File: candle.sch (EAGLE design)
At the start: 337 parts, among them U1 ATXMEGA_E5_TQFP, U3 S25FL, U4 STP16CPC26TSSOP24

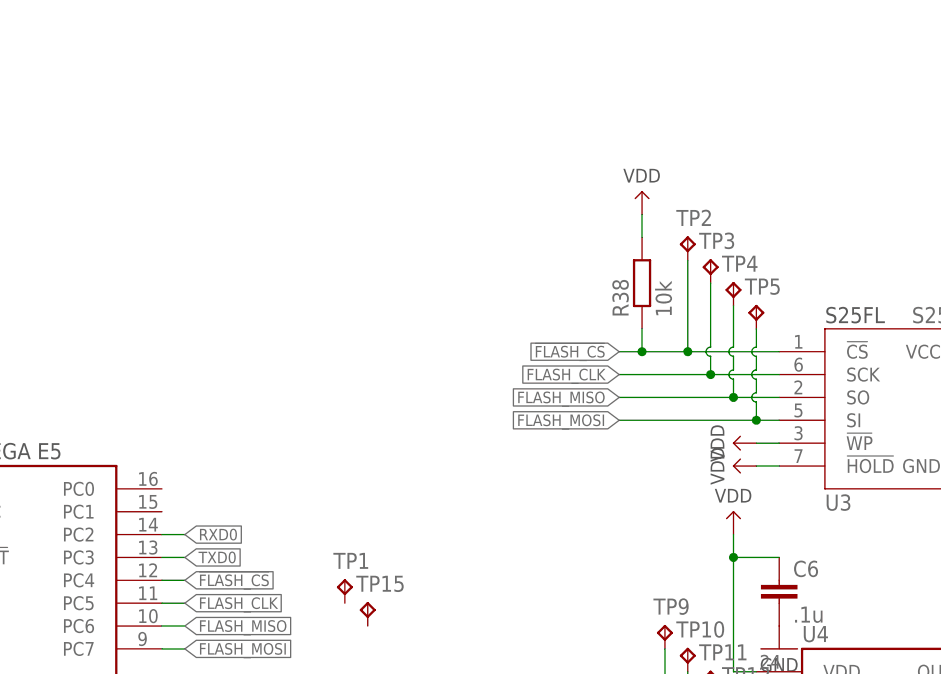
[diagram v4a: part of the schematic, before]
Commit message: Added some todos and verified the flash foodprint
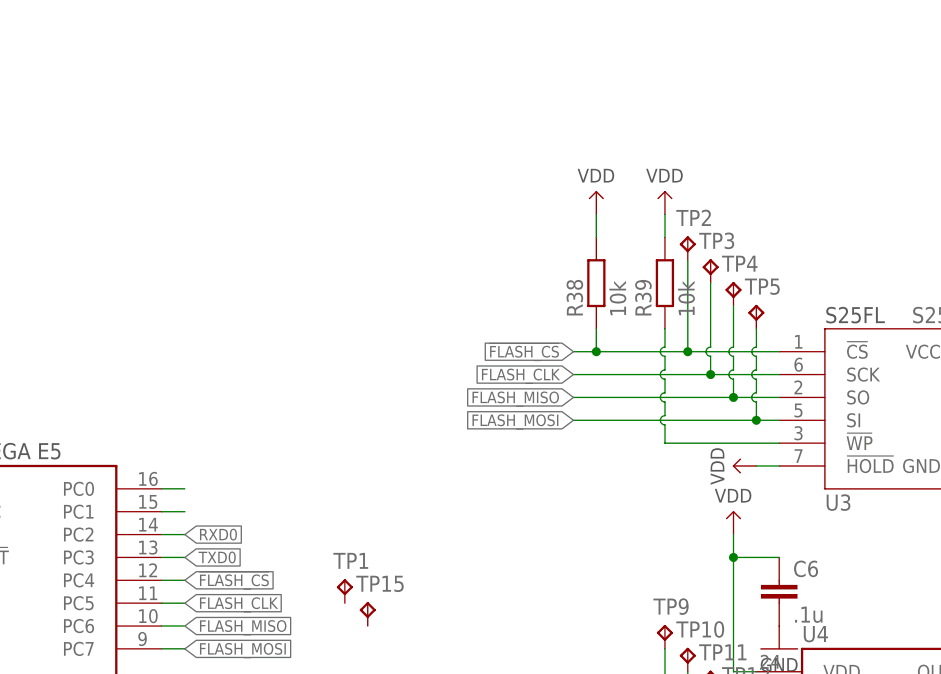
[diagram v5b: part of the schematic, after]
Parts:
- added R39: 10k, Sebastian 2:R_0603
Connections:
- new net N$15: U1.PC1
- new net N$16: U1.PC0
- new net N$6: R39.1, U3.!WP
- net VDD: now also R39.2; no longer U3.!WP
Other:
- moved on the sheet: R38
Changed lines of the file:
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@@
 <part name="P40" library="aesthetics" deviceset="VDD" device=""/>
 <part name="TP16" library="testpad" deviceset="TP" device="B1,27"/>
-<part name="P4" library="aesthetics" deviceset="VDD" device=""/>
 <part name="P5" library="aesthetics" deviceset="VDD" device=""/>
+<part name="R39" library="Sebastian 2" deviceset="R" device="_0603" value="10k"/>
+<part name="P4" library="aesthetics" deviceset="VDD" device=""/>
 </parts>
 <sheets>
@@
 <instance part="TP7" gate="G$1" x="-149.86" y="-91.44" rot="R90"/>
 <instance part="TP8" gate="G$1" x="-132.08" y="-91.44" rot="R270"/>
-<instance part="R38" gate="G$1" x="-78.74" y="30.48" rot="R90"/>
-<instance part="P40" gate="G$1" x="-78.74" y="38.1"/>
+<instance part="R38" gate="G$1" x="-83.82" y="30.48" rot="R90"/>
+<instance part="P40" gate="G$1" x="-83.82" y="38.1"/>
 <instance part="TP16" gate="G$1" x="-68.58" y="-33.02"/>
-<instance part="P4" gate="G$1" x="-66.04" y="12.7" rot="R90"/>
 <instance part="P5" gate="G$1" x="-66.04" y="10.16" rot="R90"/>
+<instance part="R39" gate="G$1" x="-76.2" y="30.48" rot="R90"/>
+<instance part="P4" gate="G$1" x="-76.2" y="38.1"/>
 </instances>
 <busses>
@@
 <segment>
 <pinref part="R38" gate="G$1" pin="2"/>
-<wire x1="-78.74" y1="38.1" x2="-78.74" y2="35.56" width="0.1524" layer="91"/>
+<wire x1="-83.82" y1="38.1" x2="-83.82" y2="35.56" width="0.1524" layer="91"/>
 <pinref part="P40" gate="G$1" pin="VDD"/>
 </segment>
 <segment>
-<pinref part="U3" gate="G$1" pin="!WP"/>
-<wire x1="-63.5" y1="12.7" x2="-66.04" y2="12.7" width="0.1524" layer="91"/>
-<pinref part="P4" gate="G$1" pin="VDD"/>
-</segment>
-<segment>
 <pinref part="U3" gate="G$1" pin="!HOLD"/>
 <wire x1="-63.5" y1="10.16" x2="-66.04" y2="10.16" width="0.1524" layer="91"/>
 <pinref part="P5" gate="G$1" pin="VDD"/>
 </segment>
+<segment>
+<pinref part="R39" gate="G$1" pin="2"/>
+<wire x1="-76.2" y1="38.1" x2="-76.2" y2="35.56" width="0.1524" layer="91"/>
+<pinref part="P4" gate="G$1" pin="VDD"/>
+</segment>
 </net>
 <net name="DISP_CLK" class="0">
@@
 <pinref part="U3" gate="G$1" pin="SCK"/>
 <wire x1="-63.5" y1="20.32" x2="-71.12" y2="20.32" width="0.1524" layer="91"/>
-<label x="-81.28" y="20.32" size="1.27" layer="95" font="vector" rot="R180" xref="yes"/>
+<label x="-86.36" y="20.32" size="1.27" layer="95" font="vector" rot="R180" xref="yes"/>
 <pinref part="TP3" gate="G$1" pin="TP"/>
-<wire x1="-71.12" y1="20.32" x2="-81.28" y2="20.32" width="0.1524" layer="91"/>
+<wire x1="-71.12" y1="20.32" x2="-86.36" y2="20.32" width="0.1524" layer="91"/>
 <wire x1="-71.12" y1="30.48" x2="-71.12" y2="23.368" width="0.1524" layer="91"/>
 <wire x1="-71.12" y1="23.368" x2="-71.628" y2="22.86" width="0.1524" layer="91" curve="90"/>
@@
 <pinref part="U3" gate="G$1" pin="SI"/>
 <wire x1="-63.5" y1="15.24" x2="-66.04" y2="15.24" width="0.1524" layer="91"/>
-<label x="-81.28" y="15.24" size="1.27" layer="95" font="vector" rot="R180" xref="yes"/>
+<label x="-86.36" y="15.24" size="1.27" layer="95" font="vector" rot="R180" xref="yes"/>
 <pinref part="TP5" gate="G$1" pin="TP"/>
-<wire x1="-66.04" y1="15.24" x2="-81.28" y2="15.24" width="0.1524" layer="91"/>
+<wire x1="-66.04" y1="15.24" x2="-86.36" y2="15.24" width="0.1524" layer="91"/>
 <wire x1="-66.04" y1="25.4" x2="-66.04" y2="23.368" width="0.1524" layer="91"/>
 <wire x1="-66.04" y1="23.368" x2="-66.548" y2="22.86" width="0.1524" layer="91" curve="90"/>
@@
 <pinref part="U3" gate="G$1" pin="!CS"/>
 <wire x1="-63.5" y1="22.86" x2="-73.66" y2="22.86" width="0.1524" layer="91"/>
-<label x="-81.28" y="22.86" size="1.27" layer="95" font="vector" rot="R180" xref="yes"/>
+<label x="-86.36" y="22.86" size="1.27" layer="95" font="vector" rot="R180" xref="yes"/>
 <pinref part="TP2" gate="G$1" pin="TP"/>
-<wire x1="-73.66" y1="22.86" x2="-78.74" y2="22.86" width="0.1524" layer="91"/>
-<wire x1="-78.74" y1="22.86" x2="-81.28" y2="22.86" width="0.1524" layer="91"/>
+<wire x1="-73.66" y1="22.86" x2="-83.82" y2="22.86" width="0.1524" layer="91"/>
+<wire x1="-83.82" y1="22.86" x2="-86.36" y2="22.86" width="0.1524" layer="91"/>
 <wire x1="-73.66" y1="33.02" x2="-73.66" y2="22.86" width="0.1524" layer="91"/>
 <junction x="-73.66" y="22.86"/>
 <pinref part="R38" gate="G$1" pin="1"/>
-<wire x1="-78.74" y1="25.4" x2="-78.74" y2="22.86" width="0.1524" layer="91"/>
-<junction x="-78.74" y="22.86"/>
+<wire x1="-83.82" y1="25.4" x2="-83.82" y2="22.86" width="0.1524" layer="91"/>
+<junction x="-83.82" y="22.86"/>
 </segment>
 <segment>
@@
 <pinref part="U3" gate="G$1" pin="SO"/>
 <wire x1="-63.5" y1="17.78" x2="-68.58" y2="17.78" width="0.1524" layer="91"/>
-<label x="-81.28" y="17.78" size="1.27" layer="95" font="vector" rot="R180" xref="yes"/>
+<label x="-86.36" y="17.78" size="1.27" layer="95" font="vector" rot="R180" xref="yes"/>
 <pinref part="TP4" gate="G$1" pin="TP"/>
-<wire x1="-68.58" y1="17.78" x2="-81.28" y2="17.78" width="0.1524" layer="91"/>
+<wire x1="-68.58" y1="17.78" x2="-86.36" y2="17.78" width="0.1524" layer="91"/>
 <wire x1="-68.58" y1="27.94" x2="-68.58" y2="23.368" width="0.1524" layer="91"/>
 <wire x1="-68.58" y1="23.368" x2="-69.088" y2="22.86" width="0.1524" layer="91" curve="90"/>
@@
 </segment>
 </net>
+<net name="N$6" class="0">
+<segment>
+<pinref part="U3" gate="G$1" pin="!WP"/>
+<pinref part="R39" gate="G$1" pin="1"/>
+<wire x1="-76.2" y1="25.4" x2="-76.2" y2="23.368" width="0.1524" layer="91"/>
+<wire x1="-76.2" y1="23.368" x2="-76.708" y2="22.86" width="0.1524" layer="91" curve="90"/>
+<wire x1="-76.708" y1="22.86" x2="-76.2" y2="22.352" width="0.1524" layer="91" curve="90"/>
+<wire x1="-76.2" y1="22.352" x2="-76.2" y2="20.828" width="0.1524" layer="91"/>
+<wire x1="-76.2" y1="20.828" x2="-76.708" y2="20.32" width="0.1524" layer="91" curve="90"/>
+<wire x1="-76.708" y1="20.32" x2="-76.2" y2="19.812" width="0.1524" layer="91" curve="90"/>
+<wire x1="-76.2" y1="19.812" x2="-76.2" y2="18.288" width="0.1524" layer="91"/>
+<wire x1="-76.2" y1="18.288" x2="-76.708" y2="17.78" width="0.1524" layer="91" curve="90"/>
+<wire x1="-76.708" y1="17.78" x2="-76.2" y2="17.272" width="0.1524" layer="91" curve="90"/>
+<wire x1="-76.2" y1="17.272" x2="-76.2" y2="15.748" width="0.1524" layer="91"/>
+<wire x1="-76.2" y1="15.748" x2="-76.708" y2="15.24" width="0.1524" layer="91" curve="90"/>
+<wire x1="-76.708" y1="15.24" x2="-76.2" y2="14.732" width="0.1524" layer="91" curve="90"/>
+<wire x1="-76.2" y1="14.732" x2="-76.2" y2="12.7" width="0.1524" layer="91"/>
+<wire x1="-63.5" y1="12.7" x2="-76.2" y2="12.7" width="0.1524" layer="91"/>
+</segment>
+</net>
+<net name="N$15" class="0">
+<segment>
+<pinref part="U1" gate="G$1" pin="PC1"/>
+<wire x1="-132.08" y1="5.08" x2="-129.54" y2="5.08" width="0.1524" layer="91"/>
+</segment>
+</net>
+<net name="N$16" class="0">
+<segment>
+<pinref part="U1" gate="G$1" pin="PC0"/>
+<wire x1="-132.08" y1="7.62" x2="-129.54" y2="7.62" width="0.1524" layer="91"/>
+</segment>
+</net>
